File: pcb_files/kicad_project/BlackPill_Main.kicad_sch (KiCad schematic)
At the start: 32 parts, among them J10 Conn_01x04_Pin, J9 Conn_01x04_Pin

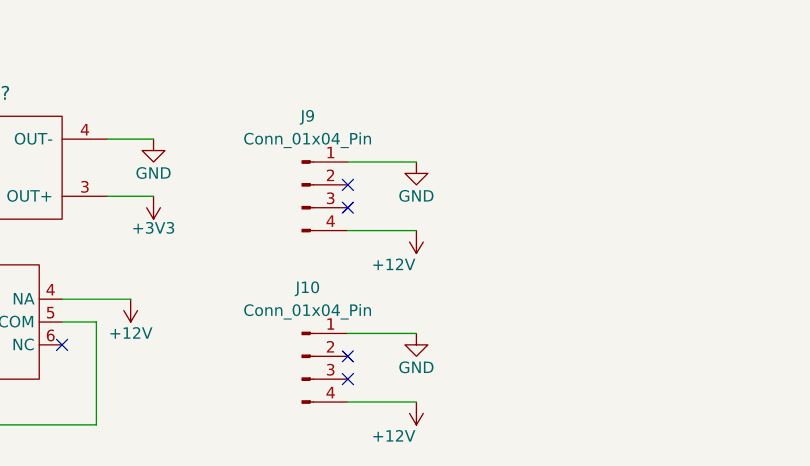
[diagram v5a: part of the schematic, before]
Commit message: Termina el diseño del esquemático y PCB
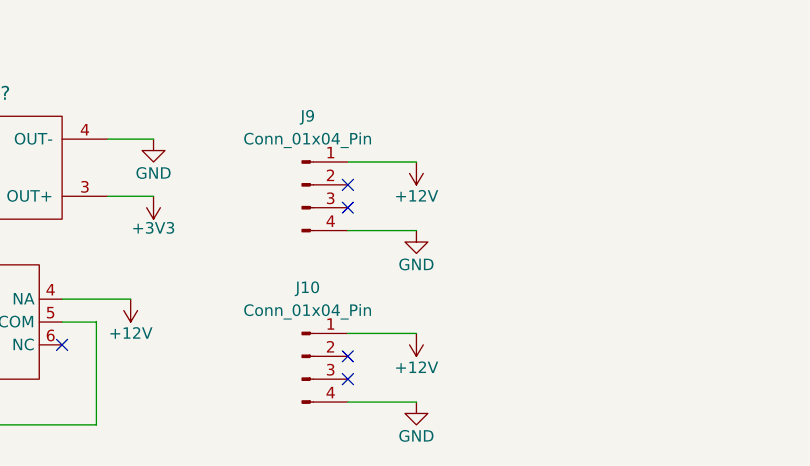
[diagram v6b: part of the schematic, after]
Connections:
- net +12V: now also J10.1 (Pin_1), J9.1 (Pin_1); no longer J10.4 (Pin_4), J9.4 (Pin_4)
- net GND: now also J10.4 (Pin_4), J9.4 (Pin_4); no longer J10.1 (Pin_1), J9.1 (Pin_1)
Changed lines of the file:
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@@
-    )
-  )
-  (symbol (lib_id "power:+12V") (at 87.63 171.45 180) (unit 1)
-    (in_bom yes) (on_board yes) (dnp no)
-    (property "Reference" "#PWR?" (at 87.63 167.64 0)
-      (effects (font (size 1.27 1.27)) hide)
-    )
-    (property "Value" "+12V" (at 85.09 175.26 0)
-      (effects (font (size 1.27 1.27)))
-    )
-    (property "Footprint" "" (at 87.63 171.45 0)
-      (effects (font (size 1.27 1.27)) hide)
-    )
-    (property "Datasheet" "" (at 87.63 171.45 0)
-      (effects (font (size 1.27 1.27)) hide)
-    )
-    (pin "1")
-    (instances
-      (project "UltiBot"
-        (path "/24197ddb-6745-4cc2-89a2-3cda2c96a453/801aac4b-54d6-4691-9ae2-22a76f924486"
-          (reference "#PWR?") (unit 1)
-        )
-        (path "/24197ddb-6745-4cc2-89a2-3cda2c96a453/922bab18-0964-4bd0-af02-17c76d29e803"
-          (reference "#PWR024") (unit 1)
-        )
-      )
     )
   )
@@
     )
   )
-  (symbol (lib_id "power:GND") (at 87.63 163.83 0) (unit 1)
-    (in_bom yes) (on_board yes) (dnp no)
-    (property "Reference" "#PWR023" (at 87.63 170.18 0)
-      (effects (font (size 1.27 1.27)) hide)
-    )
-    (property "Value" "GND" (at 87.63 167.64 0)
-      (effects (font (size 1.27 1.27)))
-    )
-    (property "Footprint" "" (at 87.63 163.83 0)
-      (effects (font (size 1.27 1.27)) hide)
-    )
-    (property "Datasheet" "" (at 87.63 163.83 0)
-      (effects (font (size 1.27 1.27)) hide)
-    )
-    (pin "1")
-    (instances
-      (project "UltiBot"
-        (path "/24197ddb-6745-4cc2-89a2-3cda2c96a453/922bab18-0964-4bd0-af02-17c76d29e803"
-          (reference "#PWR023") (unit 1)
-        )
-      )
-    )
-  )
   (symbol (lib_id "power:+12V") (at 24.13 184.15 180) (unit 1)
     (in_bom yes) (on_board yes) (dnp no)
@@
         (path "/24197ddb-6745-4cc2-89a2-3cda2c96a453/922bab18-0964-4bd0-af02-17c76d29e803"
           (reference "#PWR018") (unit 1)
+        )
+      )
+    )
+  )
+  (symbol (lib_id "power:+12V") (at 87.63 182.88 180) (unit 1)
+    (in_bom yes) (on_board yes) (dnp no)
+    (property "Reference" "#PWR?" (at 87.63 179.07 0)
+      (effects (font (size 1.27 1.27)) hide)
+    )
+    (property "Value" "+12V" (at 87.63 186.69 0)
+      (effects (font (size 1.27 1.27)))
+    )
+    (property "Footprint" "" (at 87.63 182.88 0)
+      (effects (font (size 1.27 1.27)) hide)
+    )
+    (property "Datasheet" "" (at 87.63 182.88 0)
+      (effects (font (size 1.27 1.27)) hide)
+    )
+    (pin "1")
+    (instances
+      (project "UltiBot"
+        (path "/24197ddb-6745-4cc2-89a2-3cda2c96a453/801aac4b-54d6-4691-9ae2-22a76f924486"
+          (reference "#PWR?") (unit 1)
+        )
+        (path "/24197ddb-6745-4cc2-89a2-3cda2c96a453/922bab18-0964-4bd0-af02-17c76d29e803"
+          (reference "#PWR026") (unit 1)
         )
       )
@@
         (path "/24197ddb-6745-4cc2-89a2-3cda2c96a453/922bab18-0964-4bd0-af02-17c76d29e803"
           (reference "R1") (unit 1)
+        )
+      )
+    )
+  )
+  (symbol (lib_id "power:GND") (at 87.63 171.45 0) (unit 1)
+    (in_bom yes) (on_board yes) (dnp no)
+    (property "Reference" "#PWR023" (at 87.63 177.8 0)
+      (effects (font (size 1.27 1.27)) hide)
+    )
+    (property "Value" "GND" (at 87.63 175.26 0)
+      (effects (font (size 1.27 1.27)))
+    )
+    (property "Footprint" "" (at 87.63 171.45 0)
+      (effects (font (size 1.27 1.27)) hide)
+    )
+    (property "Datasheet" "" (at 87.63 171.45 0)
+      (effects (font (size 1.27 1.27)) hide)
+    )
+    (pin "1")
+    (instances
+      (project "UltiBot"
+        (path "/24197ddb-6745-4cc2-89a2-3cda2c96a453/922bab18-0964-4bd0-af02-17c76d29e803"
+          (reference "#PWR023") (unit 1)
         )
       )
@@
     )
   )
+  (symbol (lib_id "power:+12V") (at 87.63 163.83 180) (unit 1)
+    (in_bom yes) (on_board yes) (dnp no)
+    (property "Reference" "#PWR?" (at 87.63 160.02 0)
+      (effects (font (size 1.27 1.27)) hide)
+    )
+    (property "Value" "+12V" (at 87.63 167.64 0)
+      (effects (font (size 1.27 1.27)))
+    )
+    (property "Footprint" "" (at 87.63 163.83 0)
+      (effects (font (size 1.27 1.27)) hide)
+    )
+    (property "Datasheet" "" (at 87.63 163.83 0)
+      (effects (font (size 1.27 1.27)) hide)
+    )
+    (pin "1")
+    (instances
+      (project "UltiBot"
+        (path "/24197ddb-6745-4cc2-89a2-3cda2c96a453/801aac4b-54d6-4691-9ae2-22a76f924486"
+          (reference "#PWR?") (unit 1)
+        )
+        (path "/24197ddb-6745-4cc2-89a2-3cda2c96a453/922bab18-0964-4bd0-af02-17c76d29e803"
+          (reference "#PWR024") (unit 1)
+        )
+      )
+    )
+  )
   (symbol (lib_id "power:GND") (at 46.99 128.27 0) (unit 1)
     (in_bom yes) (on_board yes) (dnp no)
@@
     )
   )
-  (symbol (lib_id "power:+12V") (at 87.63 190.5 180) (unit 1)
-    (in_bom yes) (on_board yes) (dnp no)
-    (property "Reference" "#PWR?" (at 87.63 186.69 0)
-      (effects (font (size 1.27 1.27)) hide)
-    )
-    (property "Value" "+12V" (at 85.09 194.31 0)
-      (effects (font (size 1.27 1.27)))
-    )
-    (property "Footprint" "" (at 87.63 190.5 0)
-      (effects (font (size 1.27 1.27)) hide)
-    )
-    (property "Datasheet" "" (at 87.63 190.5 0)
+  (symbol (lib_id "power:+12V") (at 55.88 179.07 180) (unit 1)
+    (in_bom yes) (on_board yes) (dnp no)
+    (property "Reference" "#PWR?" (at 55.88 175.26 0)
+      (effects (font (size 1.27 1.27)) hide)
+    )
+    (property "Value" "+12V" (at 55.88 182.88 0)
+      (effects (font (size 1.27 1.27)))
+    )
+    (property "Footprint" "" (at 55.88 179.07 0)
+      (effects (font (size 1.27 1.27)) hide)
+    )
+    (property "Datasheet" "" (at 55.88 179.07 0)
       (effects (font (size 1.27 1.27)) hide)
     )
@@
         )
         (path "/24197ddb-6745-4cc2-89a2-3cda2c96a453/922bab18-0964-4bd0-af02-17c76d29e803"
-          (reference "#PWR026") (unit 1)
-        )
-      )
-    )
-  )
-  (symbol (lib_id "power:+12V") (at 55.88 179.07 180) (unit 1)
-    (in_bom yes) (on_board yes) (dnp no)
-    (property "Reference" "#PWR?" (at 55.88 175.26 0)
-      (effects (font (size 1.27 1.27)) hide)
-    )
-    (property "Value" "+12V" (at 55.88 182.88 0)
-      (effects (font (size 1.27 1.27)))
-    )
-    (property "Footprint" "" (at 55.88 179.07 0)
-      (effects (font (size 1.27 1.27)) hide)
-    )
-    (property "Datasheet" "" (at 55.88 179.07 0)
-      (effects (font (size 1.27 1.27)) hide)
-    )
-    (pin "1")
-    (instances
-      (project "UltiBot"
-        (path "/24197ddb-6745-4cc2-89a2-3cda2c96a453/801aac4b-54d6-4691-9ae2-22a76f924486"
-          (reference "#PWR?") (unit 1)
-        )
-        (path "/24197ddb-6745-4cc2-89a2-3cda2c96a453/922bab18-0964-4bd0-af02-17c76d29e803"
           (reference "#PWR019") (unit 1)
         )
@@
     )
   )
+  (symbol (lib_id "power:GND") (at 87.63 190.5 0) (unit 1)
+    (in_bom yes) (on_board yes) (dnp no)
+    (property "Reference" "#PWR025" (at 87.63 196.85 0)
+      (effects (font (size 1.27 1.27)) hide)
+    )
+    (property "Value" "GND" (at 87.63 194.31 0)
+      (effects (font (size 1.27 1.27)))
+    )
+    (property "Footprint" "" (at 87.63 190.5 0)
+      (effects (font (size 1.27 1.27)) hide)
+    )
+    (property "Datasheet" "" (at 87.63 190.5 0)
+      (effects (font (size 1.27 1.27)) hide)
+    )
+    (pin "1")
+    (instances
+      (project "UltiBot"
+        (path "/24197ddb-6745-4cc2-89a2-3cda2c96a453/922bab18-0964-4bd0-af02-17c76d29e803"
+          (reference "#PWR025") (unit 1)
+        )
+      )
+    )
+  )
   (symbol (lib_id "power:GND") (at 280.67 55.88 0) (unit 1)
     (in_bom yes) (on_board yes) (dnp no) (fields_autoplaced)
@@
         )
       )
-    )
-  )
-  (symbol (lib_id "power:GND") (at 87.63 182.88 0) (unit 1)
-    (in_bom yes) (on_board yes) (dnp no)
-    (property "Reference" "#PWR025" (at 87.63 189.23 0)
-      (effects (font (size 1.27 1.27)) hide)
-    )
-    (property "Value" "GND" (at 87.63 186.69 0)
-      (effects (font (size 1.27 1.27)))
-    )
-    (property "Footprint" "" (at 87.63 182.88 0)
-      (effects (font (size 1.27 1.27)) hide)
-    )
-    (property "Datasheet" "" (at 87.63 182.88 0)
-      (effects (font (size 1.27 1.27)) hide)
-    )
-    (pin "1")
-    (instances
-      (project "UltiBot"
-        (path "/24197ddb-6745-4cc2-89a2-3cda2c96a453/922bab18-0964-4bd0-af02-17c76d29e803"
-          (reference "#PWR025") (unit 1)
-        )
-      )
